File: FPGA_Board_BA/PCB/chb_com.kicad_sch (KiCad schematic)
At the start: 9 parts, among them J12 Box_Header_2x05_THT, J13 Box_Header_2x05_THT, J14 Box_Header_2x05_THT, J15 Box_Header_2x05_THT, J18 Plug_Terminal_2x12pin, U26 BoxHeader_24pin, U45 BoxHeader_24pin, U46 BoxHeader_24pin, U47 BoxHeader_24pin

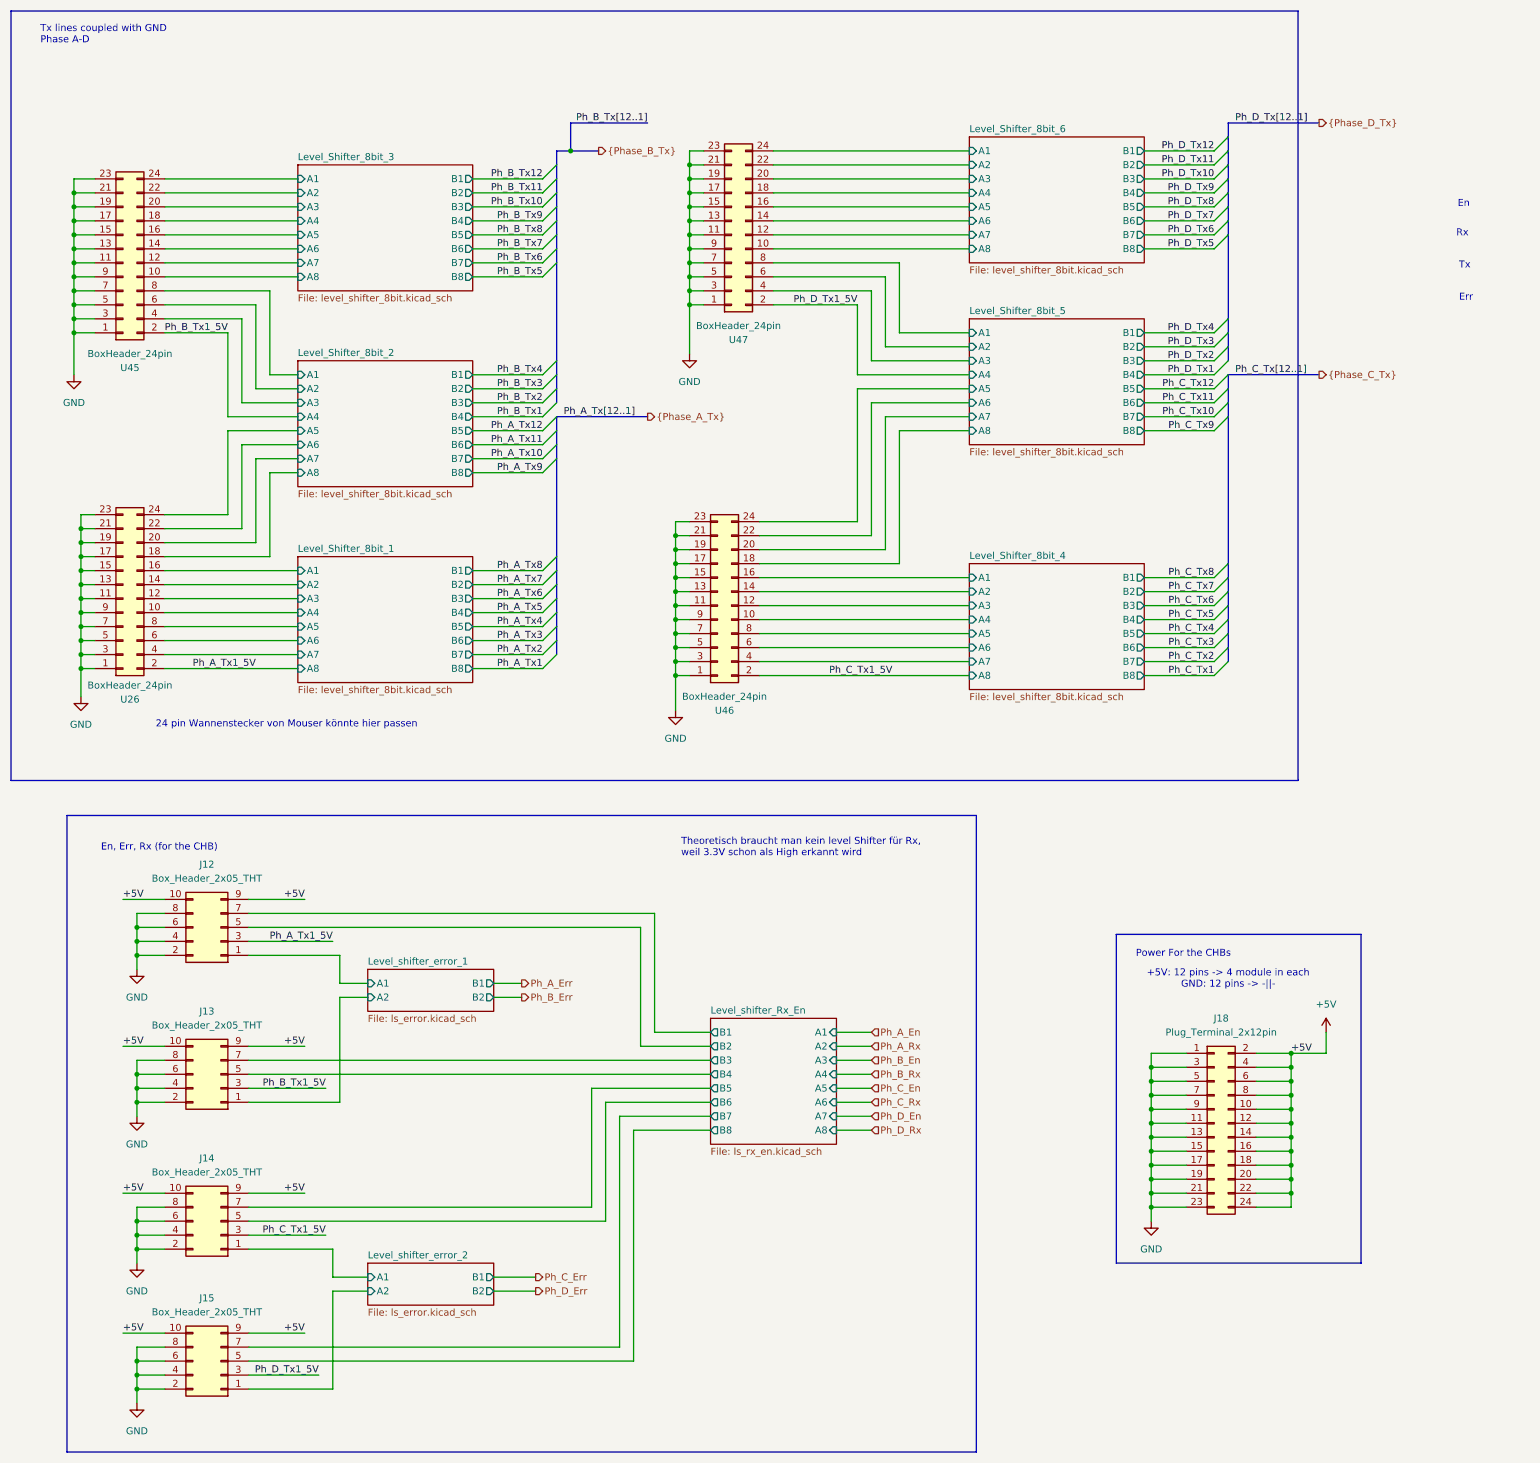
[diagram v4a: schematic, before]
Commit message: big schematic cleanup. Added wire to bus
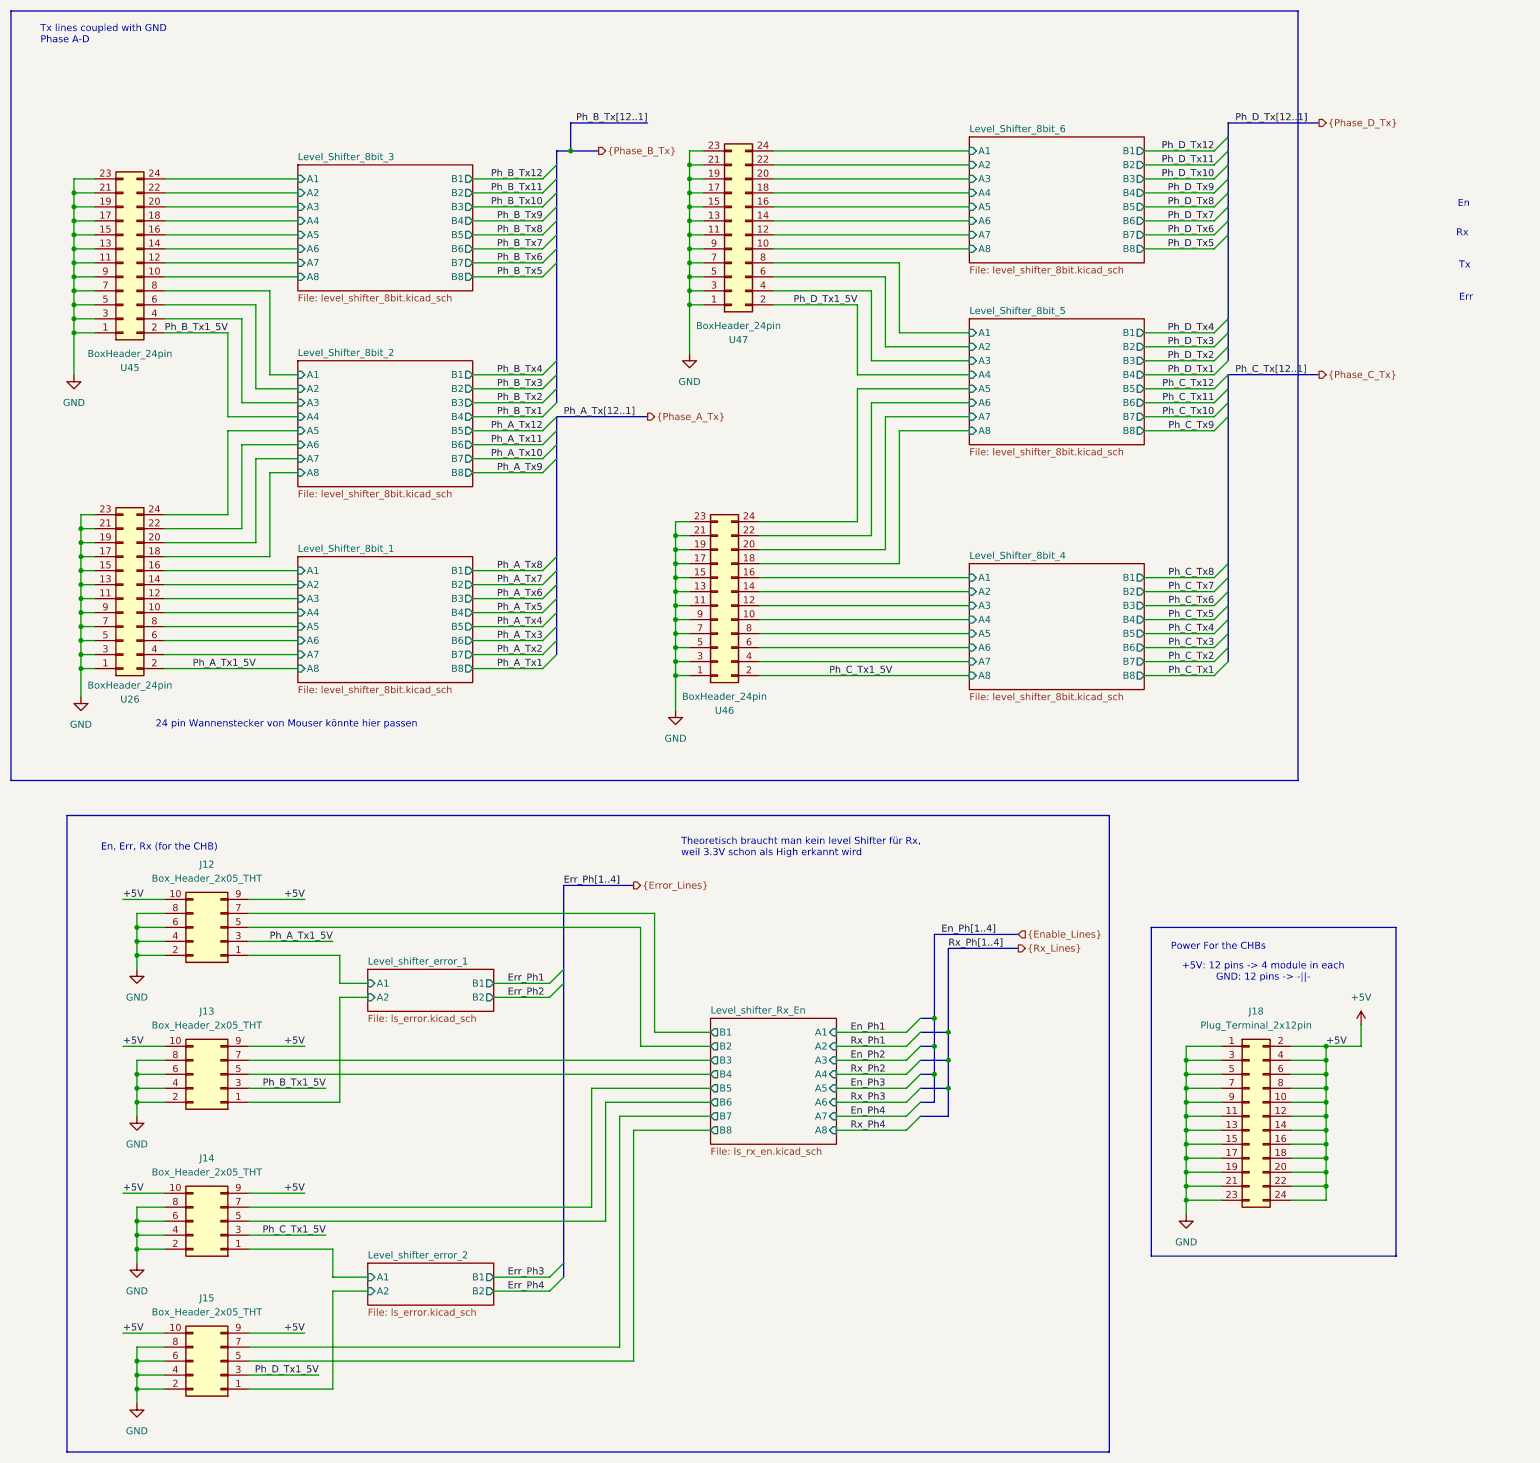
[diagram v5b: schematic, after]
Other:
- moved on the sheet: J18

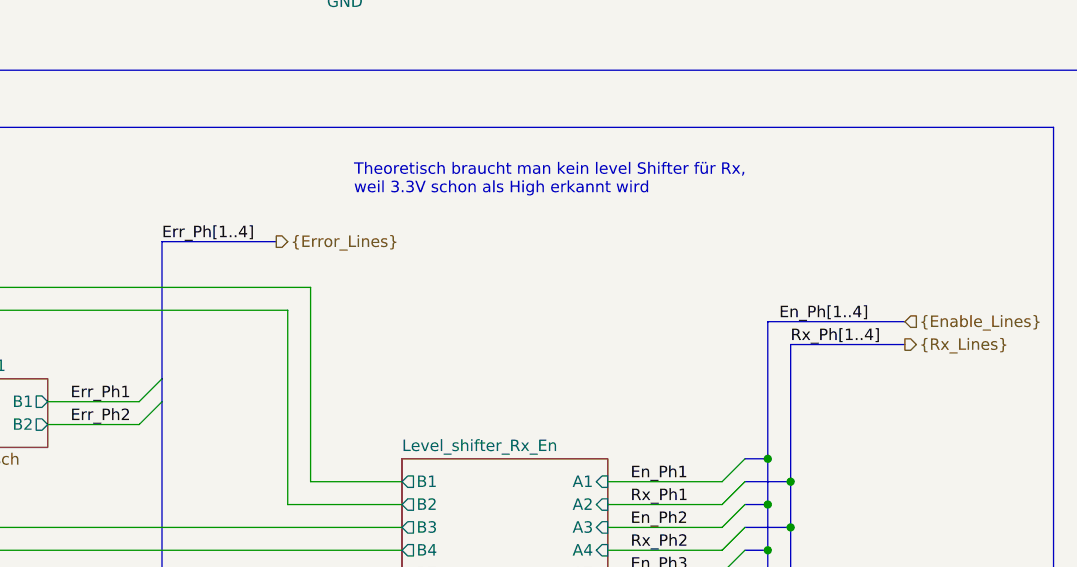
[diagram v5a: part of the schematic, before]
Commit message: fixed wire bus in schematic + routing almost ready, only routing of power is left
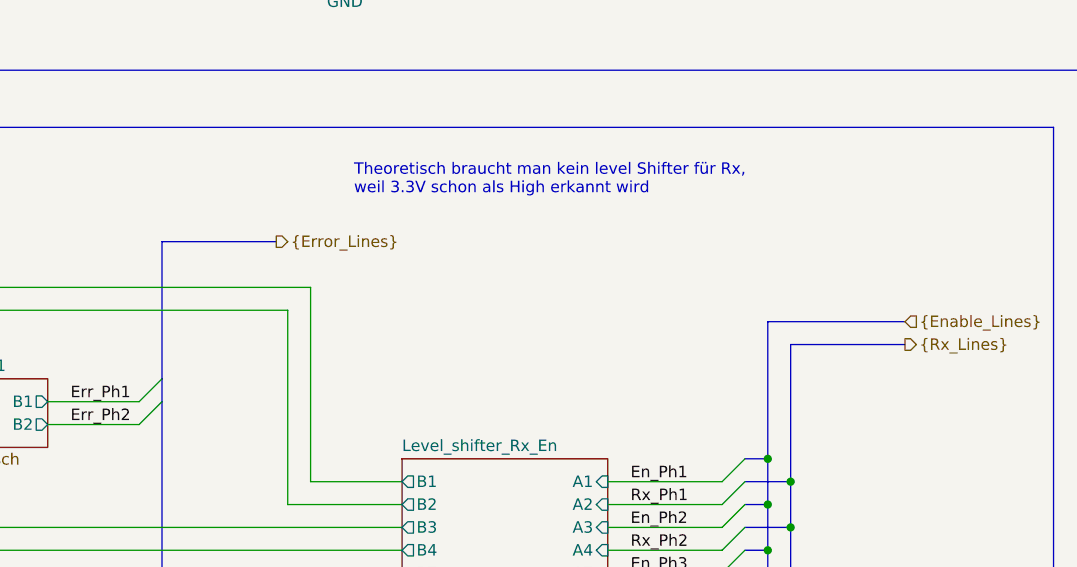
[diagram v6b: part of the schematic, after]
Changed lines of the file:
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@@
 	(generator_version "9.0")
 	(paper "A3")
+	(bus_alias "Enable_Lines"
+		(members "En_Ph1" "En_Ph2" "En_Ph3" "En_Ph4")
+	)
+	(bus_alias "Error_Lines"
+		(members "Err_Ph1" "Err_Ph2" "Err_Ph3" "Err_Ph4")
+	)
+	(bus_alias "Rx_Lines"
+		(members "Rx_Ph1" "Rx_Ph2" "Rx_Ph3" "Rx_Ph4")
+	)
 	(rectangle
 		(start 224.79 181.61)
@@
 		)
 	)
-	(label "Rx_Ph[1..4]"
-		(at 187.96 185.42 0)
-		(effects
-			(font
-				(size 1.27 1.27)
-			)
-			(justify left bottom)
-		)
-	)
 	(label "Ph_A_Tx2"
 		(at 114.3 132.08 180)
@@
 		)
 	)
-	(label "En_Ph[1..4]"
-		(at 186.69 182.88 0)
-		(effects
-			(font
-				(size 1.27 1.27)
-			)
-			(justify left bottom)
-		)
-	)
 	(label "Ph_B_Tx3"
 		(at 114.3 83.82 180)
@@
 		)
 	)
-	(label "Err_Ph[1..4]"
-		(at 118.11 173.99 0)
-		(effects
-			(font
-				(size 1.27 1.27)
-			)
-			(justify left bottom)
-		)
-	)
